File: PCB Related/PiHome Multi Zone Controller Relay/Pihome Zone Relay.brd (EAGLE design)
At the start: 100 x 78.7 mm, 17 parts, among them IC1 REG1117, M1 WIRELESS-NRF24L01, M3 ARDUINO-PRO-MINI-5.0V

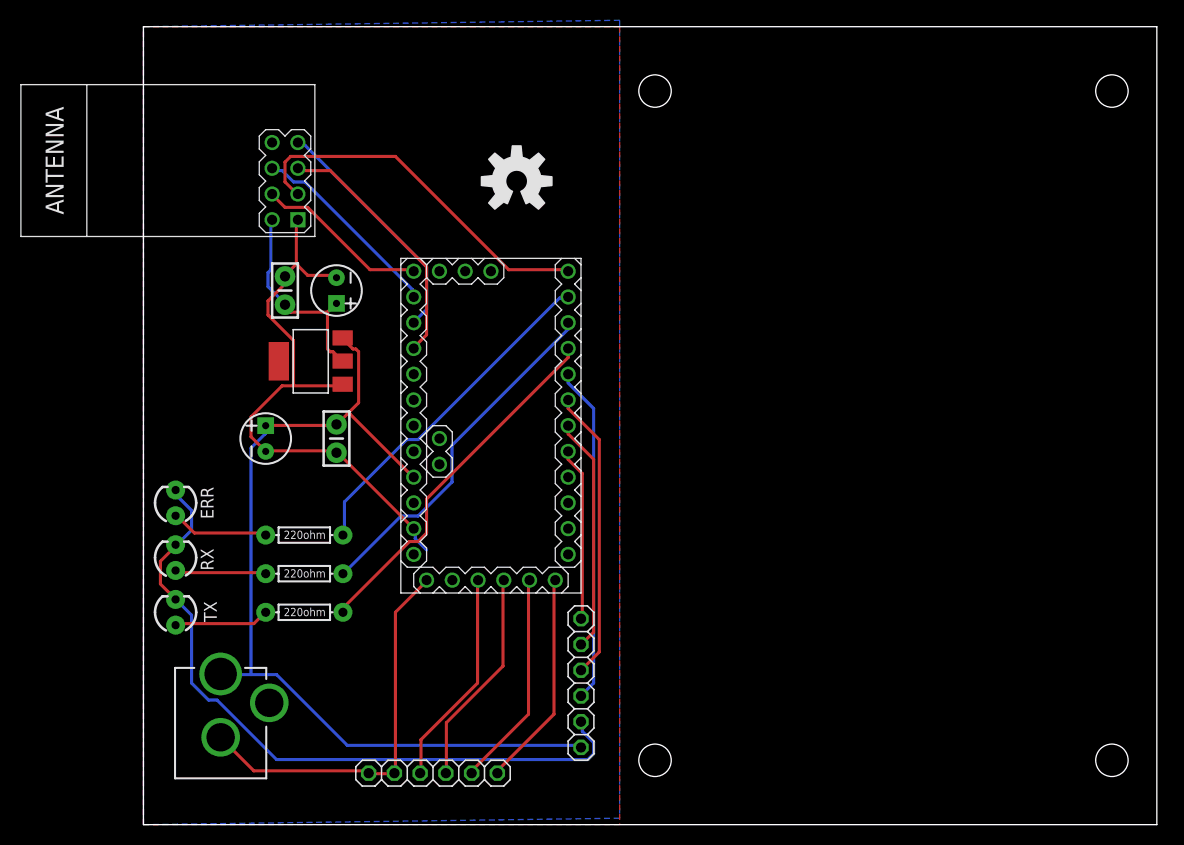
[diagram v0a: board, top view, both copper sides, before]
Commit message: PiHome – Smart Heating Controller
PCB improvements
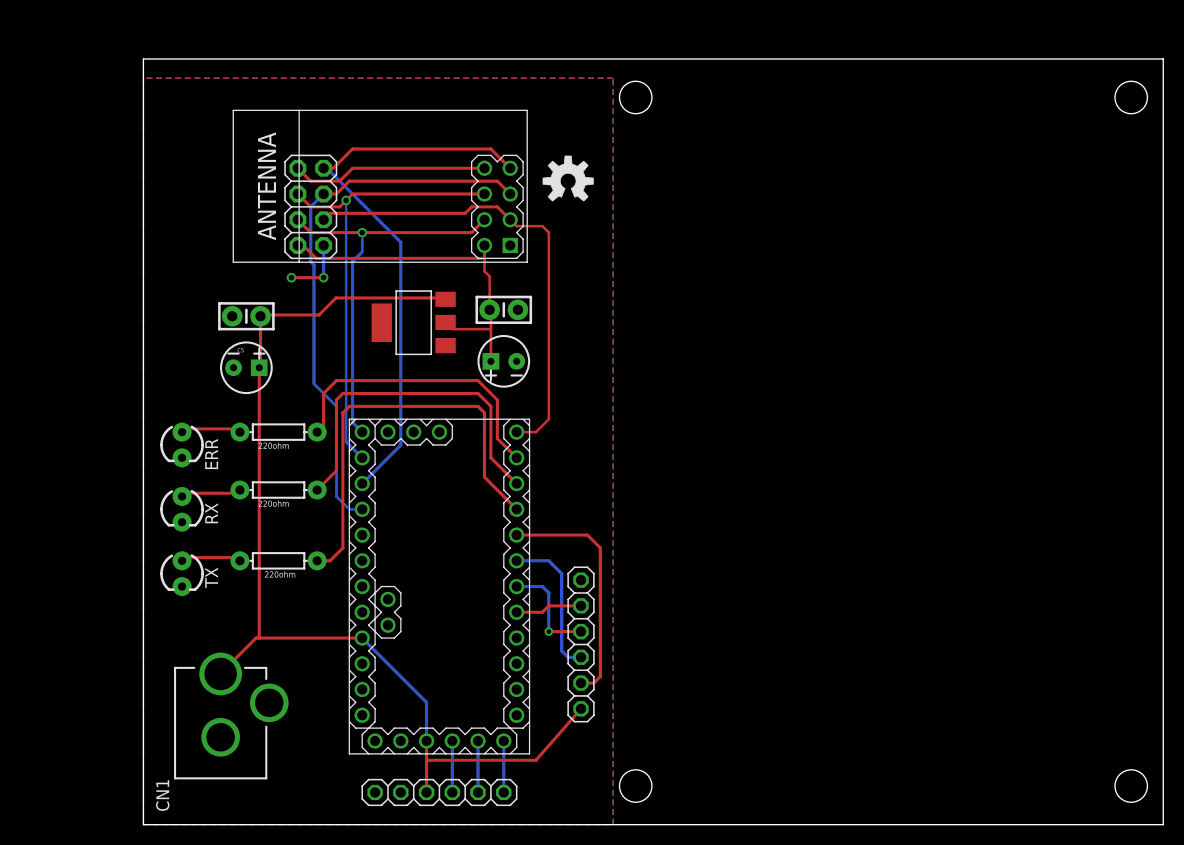
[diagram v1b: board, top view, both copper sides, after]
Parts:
- removed LOGO1: OSHW-LOGOL, SparkFun-Aesthetics:OSHW-LOGO-L
- added JP3: (no value), adafruit:2X04
- added LOGO4: OSHW-LOGOM, SparkFun-Aesthetics:OSHW-LOGO-M
- moved C4 21.7 mm to (35.6, 50.8), turned to 0 degrees
- moved M1 21.1 mm to (23.5, 63.5)
- moved C6 17.9 mm to (35.6, 45.7), turned to 180 degrees
- moved M3 16.7 mm to (29.2, 23.5)
- moved C3 15.0 mm to (10.2, 50.2), turned to 180 degrees
- moved IC1 10.9 mm to (26.7, 49.5)
- moved R4 10.5 mm to (13.3, 38.7)
- moved R3 8.64 mm to (13.3, 33.0)
- moved C5 7.24 mm to (10.2, 45.1), turned to 0 degrees
- moved ERR 5.75 mm to (3.81, 37.5), turned to 270 degrees
- moved R2 5.68 mm to (13.3, 26.0)
- moved RX 4.80 mm to (3.81, 31.1), turned to 270 degrees
- moved TX 3.86 mm to (3.81, 24.8), turned to 270 degrees
- moved JP2 3.81 mm to (43.2, 17.8)
- moved JP1 2.01 mm to (29.2, 3.17)
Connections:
- removed net GND-: C3.2, C4.2, C5.2, C6.2, CN1.GND, IC1.1, JP1.5, JP1.6, M3.J6.2
- removed net GND.1: M3.J7.9
- removed net GNDBREAK: CN1.GNDBREAK
- removed net PC_VCC: JP1.4, M3.J1.3
- net CE: now also JP3.3
- net CSN: now also JP3.4
- net GND: now also C3.2, C4.2, C5.2, C6.2, CN1.GND, CN1.GNDBREAK, IC1.1, JP1.5, JP1.6, JP2.1, JP3.1, M3.J1.2, M3.J6.2, M3.J7.9; no longer JP2.5
- net IN01: now also JP2.2; no longer JP2.1
- net IN02: now also JP2.3; no longer JP2.2
- net IN03: now also JP2.4; no longer JP2.3
- net IN04: now also JP2.5
- net IRQ: now also JP3.8
- net MISO: now also JP3.7
- net MOSI: now also JP3.6
- net SCK: now also JP3.5
- net VCC_3.3: now also JP3.2
- net VCC_5: now also JP1.4, M3.J1.3
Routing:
- net GND-: track 96.8 -> 0.00 mm
- net GND: track 68.9 -> 6.35 mm, vias 0 -> 2
- net MISO: track 23.9 -> 56.0 mm
- net SCK: track 25.3 -> 54.0 mm
- net MOSI: track 19.6 -> 45.5 mm, vias 0 -> 1
- net CSN: track 17.2 -> 39.9 mm, vias 0 -> 1
- net PC_VCC: track 21.4 -> 0.00 mm
- net IRQ: track 0.00 -> 19.5 mm
- net DTR: track 21.4 -> 5.08 mm
- net TXD: track 21.4 -> 5.08 mm
- net RXD: track 21.4 -> 5.08 mm
- net VCC_3.3: track 20.7 -> 35.4 mm
- net IN03: track 28.7 -> 14.8 mm
- net IN02: track 23.2 -> 10.6 mm, vias 0 -> 1
- net VCC_5: track 90.1 -> 101.7 mm
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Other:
- board size 100 x 78.7 mm -> 100.6 x 75.6 mm
- board text added: "4 Channel SainSmart Relay Board"
- board text added: "DTR"
- board text added: "GND"
- board text added: "RXD"
- board text added: "TXD"
- board text added: "vcc"
- board text removed: "nRF24L01 / 2.4GHz RF"

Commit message: Improved PCB Design
Improved PCB Design
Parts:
- removed JP1: (no value), adafruit:1X06
- removed M3: ARDUINO-PRO-MINI-5.0V, diy-modules:ARDUINO-PRO-MINI
- added C1: 10uf, SparkFun-Capacitors:CPOL-RADIAL-10UF-25V-KIT
- added U$1: NANO, Arduino Pro Mini-Nano:NANO
- added U$2: MICRO-USB, microusb:MICRO-USB
- moved CN1 5.46 mm to (10.8, -3.17)
- moved IC1 3.18 mm to (26.7, 46.4)
- moved JP2 3.18 mm to (43.2, 14.6), turned to 90 degrees
- moved C6 2.22 mm to (35.6, 43.5)
- moved C4 1.90 mm to (35.6, 48.9)
- moved LOGO4 1.27 mm to (41.9, 64.8)
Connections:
- removed net DTR: JP1.1, M3.J1.6
- removed net IN01: JP2.2, M3.J7.8
- removed net IN02: JP2.3, M3.J7.7
- removed net IN03: JP2.4, M3.J7.6
- removed net IN04: JP2.5, M3.J7.5
- removed net RAW: M3.J6.1
- removed net RXD: JP1.3, M3.J1.4
- removed net TXD: JP1.2, M3.J1.5
- new net ZONE_01: JP2.2, U$1.D2
- new net ZONE_02: JP2.3, U$1.D3
- new net ZONE_03: JP2.4, U$1.D4
- new net ZONE_04: JP2.5, U$1.D5
- net CE: now also U$1.D9; no longer M3.J7.1
- net CSN: now also U$1.D10; no longer M3.J6.12
- net ERR_LED: now also U$1.D8; no longer M3.J7.2
- net GND: now also C1.2, U$1.GND, U$1.GND1, U$2.5, U$2.GND1, U$2.GND2; no longer JP1.5, JP1.6, M3.J1.1, M3.J1.2, M3.J6.2, M3.J7.9
- net MISO: now also U$1.D12; no longer M3.J6.10
- net MOSI: now also U$1.D11; no longer M3.J6.11
- net RX_LED: now also U$1.D7; no longer M3.J7.3
- net SCK: now also U$1.D13; no longer M3.J6.9
- net TX_LED: now also U$1.D6; no longer M3.J7.4
- net VCC_3.3: now also C1.1
- net VCC_5: now also U$1.5V, U$2.1; no longer JP1.4, M3.J1.3, M3.J6.4
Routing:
- net MISO: track 56.0 -> 111.5 mm
- net CSN: track 39.9 -> 81.9 mm
- net SCK: track 54.0 -> 90.3 mm
- net MOSI: track 45.5 -> 78.6 mm, vias 1 -> 0
- net TX_LED: track 41.7 -> 10.9 mm
- net ZONE_01: track 0.00 -> 28.2 mm, vias 0 -> 1
- net ZONE_02: track 0.00 -> 24.7 mm
- net CE: track 46.3 -> 70.8 mm
- net IN04: track 23.6 -> 0.00 mm
- net ZONE_03: track 0.00 -> 22.6 mm, vias 0 -> 1
- net ZONE_04: track 0.00 -> 20.5 mm
- net IN03: track 14.8 -> 0.00 mm
- net RX_LED: track 34.4 -> 22.0 mm
- net VCC_5: track 101.7 -> 112.8 mm
- net IN02: track 10.6 -> 0.00 mm, vias 1 -> 0
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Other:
- board size 100.6 x 75.6 mm -> 46.3 x 73 mm
- board text added: "0.1uF"
- board text added: "1"
- board text added: "10 uF"
- board text added: "10uF"
- board text added: "2"
- board text added: "3"
- board text added: "4"
- board text added: "Arduino Nano 5v"
- board text added: "LM1117"
- board text added: "Micro USB"
- board text added: "Multi Zone Controller Relay"
- board text added: "PiHome Smart Heating"
- board text added: "Rely Connection"
- board text added: "http://www.pihome.eu"
- board text added: "nRF24L01 / 2.4GHz"
- board text removed: "4 Channel SainSmart Relay Board"
- board text removed: "DTR"
- board text removed: "RXD"
- board text removed: "TXD"
